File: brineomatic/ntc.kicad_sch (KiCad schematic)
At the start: 4 parts, among them J3 THERMISTOR

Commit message: starting to shape up, footprints etc
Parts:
- J4: renamed from J3; footprint (none) -> TerminalBlock_Phoenix:TerminalBlock_Phoenix_PT-1,5-2-3.5-H_1x02_P3.50mm_Horizontal
- renumbered R8 to R10, R7 to R9
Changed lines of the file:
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@@
 		(dnp no)
 		(fields_autoplaced yes)
-		(property "Reference" "J3"
+		(property "Reference" "J4"
 			(at 102.87 77.47 0)
 			(effects
@@
 			)
 		)
-		(property "Footprint" ""
+		(property "Footprint" "TerminalBlock_Phoenix:TerminalBlock_Phoenix_PT-1,5-2-3.5-H_1x02_P3.50mm_Horizontal"
 			(at 102.87 83.82 0)
 			(effects
@@
 			(project ""
 				(path "/96477ae2-ef08-48f3-8dd4-fe4478541f68/a25af3cd-6e30-4758-861f-193b34fc4628"
-					(reference "J3")
+					(reference "J4")
 					(unit 1)
 				)
@@
 		(dnp no)
 		(fields_autoplaced yes)
-		(property "Reference" "#PWR09"
+		(property "Reference" "#PWR014"
 			(at 118.11 113.03 0)
 			(effects
@@
 			(project "brineomatic"
 				(path "/96477ae2-ef08-48f3-8dd4-fe4478541f68/a25af3cd-6e30-4758-861f-193b34fc4628"
-					(reference "#PWR09")
+					(reference "#PWR014")
 					(unit 1)
 				)
@@
 		(dnp no)
 		(fields_autoplaced yes)
-		(property "Reference" "R8"
+		(property "Reference" "R10"
 			(at 118.11 80.01 90)
 			(effects
@@
 			(project "brineomatic"
 				(path "/96477ae2-ef08-48f3-8dd4-fe4478541f68/a25af3cd-6e30-4758-861f-193b34fc4628"
-					(reference "R8")
+					(reference "R10")
 					(unit 1)
 				)
@@
 		(dnp no)
 		(fields_autoplaced yes)
-		(property "Reference" "R7"
+		(property "Reference" "R9"
 			(at 114.3 93.98 0)
 			(effects
@@
 			(project "brineomatic"
 				(path "/96477ae2-ef08-48f3-8dd4-fe4478541f68/a25af3cd-6e30-4758-861f-193b34fc4628"
-					(reference "R7")
+					(reference "R9")
 					(unit 1)
 				)
@@
 		(dnp no)
 		(fields_autoplaced yes)
-		(property "Reference" "#PWR08"
+		(property "Reference" "#PWR013"
 			(at 111.76 78.74 0)
 			(effects
@@
 			(project ""
 				(path "/96477ae2-ef08-48f3-8dd4-fe4478541f68/a25af3cd-6e30-4758-861f-193b34fc4628"
-					(reference "#PWR08")
-					(unit 1)
-				)
+					(reference "#PWR013")
+					(unit 1)
+				)

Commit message: starting to look good.
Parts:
- J4: footprint TerminalBlock_Phoenix:TerminalBlock_Phoenix_PT-1,5-2-3.5-H_1x02_P3.50mm_Horizontal -> Connector_JST:JST_PH_S2B-PH-K_1x02_P2.00mm_Horizontal
- R9: footprint Resistor_SMD:R_1206_3216Metric_Pad1.30x1.75mm_HandSolder -> Resistor_SMD:R_0805_2012Metric_Pad1.20x1.40mm_HandSolder
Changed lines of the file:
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@@
 			)
 		)
-		(property "Footprint" "TerminalBlock_Phoenix:TerminalBlock_Phoenix_PT-1,5-2-3.5-H_1x02_P3.50mm_Horizontal"
+		(property "Footprint" "Connector_JST:JST_PH_S2B-PH-K_1x02_P2.00mm_Horizontal"
 			(at 102.87 83.82 0)
 			(effects
@@
 			)
 		)
-		(property "Footprint" "Resistor_SMD:R_1206_3216Metric_Pad1.30x1.75mm_HandSolder"
+		(property "Footprint" "Resistor_SMD:R_0805_2012Metric_Pad1.20x1.40mm_HandSolder"
 			(at 111.76 95.25 0)
 			(effects

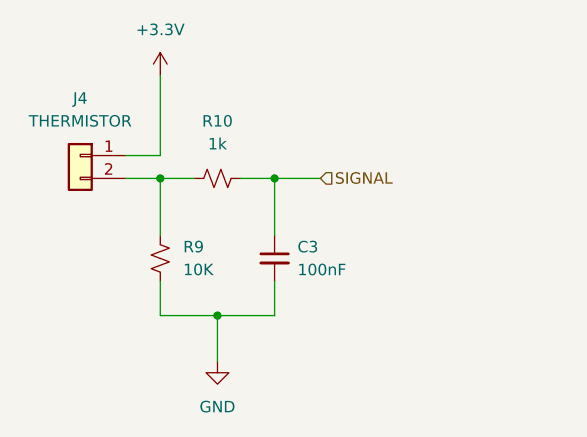
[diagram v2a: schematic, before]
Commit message: updated bom and prepping for Rev A
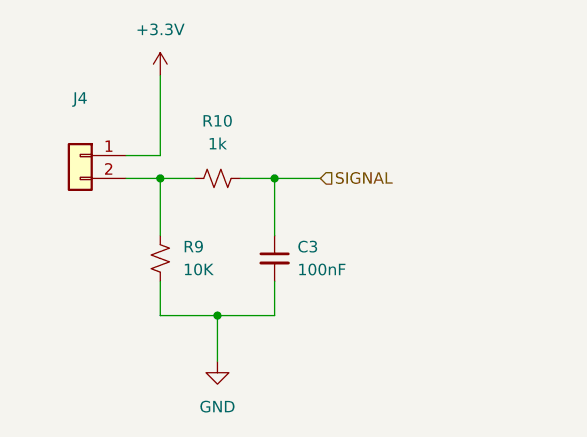
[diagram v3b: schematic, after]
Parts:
- J4: value THERMISTOR -> ~; LCSC (none) -> C173752
- R9: LCSC (none) -> C84376
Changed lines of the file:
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@@
 			)
 		)
-		(property "Value" "THERMISTOR"
+		(property "Value" "~"
 			(at 102.87 80.01 0)
 			(effects
@@
 		)
 		(property "Description" "Generic connector, single row, 01x02, script generated (kicad-library-utils/schlib/autogen/connector/)"
+			(at 102.87 83.82 0)
+			(effects
+				(font
+					(size 1.27 1.27)
+				)
+				(hide yes)
+			)
+		)
+		(property "LCSC" "C173752"
 			(at 102.87 83.82 0)
 			(effects
@@
 			)
 		)
-		(property "LCSC" ""
+		(property "LCSC" "C84376"
 			(at 111.76 95.25 0)
 			(effects

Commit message: fixed bat54s placement.
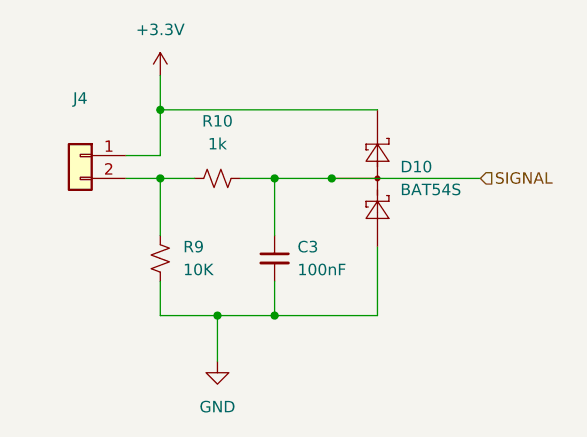
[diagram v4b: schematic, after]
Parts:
- added D10: BAT54S, Package_TO_SOT_SMD:SOT-23, symbol Diode:BAT54S
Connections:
- net +3.3V: now also D10.2 (K)
- net GND: now also D10.1 (A)
- net SIGNAL: now also D10.3 (COM)
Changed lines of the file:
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@@
+	)
+	(junction
+		(at 111.76 78.74)
+		(diameter 0)
+		(color 0 0 0 0)
+	)
+	(junction
+		(at 124.46 101.6)
+		(diameter 0)
+		(color 0 0 0 0)
 	)
 	(junction
@@
 		(color 0 0 0 0)
 	)
+	(junction
+		(at 130.81 86.36)
+		(diameter 0)
+		(color 0 0 0 0)
+	)
+	(wire
+		(pts
+			(xy 111.76 78.74) (xy 111.76 83.82)
+		)
+		(stroke
+			(width 0)
+			(type default)
+		)
+	)
 	(wire
 		(pts
@@
 	(wire
 		(pts
+			(xy 111.76 78.74) (xy 135.89 78.74)
+		)
+		(stroke
+			(width 0)
+			(type default)
+		)
+	)
+	(wire
+		(pts
 			(xy 118.11 101.6) (xy 124.46 101.6)
 		)
@@
 	(wire
 		(pts
-			(xy 111.76 74.93) (xy 111.76 83.82)
+			(xy 111.76 74.93) (xy 111.76 78.74)
 		)
 		(stroke
@@
 	(wire
 		(pts
-			(xy 124.46 86.36) (xy 129.54 86.36)
+			(xy 124.46 86.36) (xy 130.81 86.36)
 		)
 		(stroke
@@
 	(wire
 		(pts
+			(xy 130.81 86.36) (xy 147.32 86.36)
+		)
+		(stroke
+			(width 0)
+			(type default)
+		)
+	)
+	(wire
+		(pts
 			(xy 118.11 106.68) (xy 118.11 101.6)
+		)
+		(stroke
+			(width 0)
+			(type default)
+		)
+	)
+	(wire
+		(pts
+			(xy 135.89 93.98) (xy 135.89 101.6)
+		)
+		(stroke
+			(width 0)
+			(type default)
+		)
+	)
+	(wire
+		(pts
+			(xy 135.89 101.6) (xy 124.46 101.6)
 		)
 		(stroke
@@
 	(hierarchical_label "SIGNAL"
 		(shape input)
-		(at 129.54 86.36 0)
+		(at 147.32 86.36 0)
 		(fields_autoplaced yes)
 		(effects
@@
 					(unit 1)
 				)
+			)
+		)
+	)
+	(symbol
+		(lib_id "Diode:BAT54S")
+		(at 135.89 86.36 270)
+		(mirror x)
+		(unit 1)
+		(exclude_from_sim no)
+		(in_bom yes)
+		(on_board yes)
+		(dnp no)
+		(fields_autoplaced yes)
+		(property "Reference" "D10"
+			(at 138.43 85.09 90)
+			(effects
+				(font
+					(size 1.27 1.27)
+				)
+				(justify left)
+			)
+		)
+		(property "Value" "BAT54S"
+			(at 138.43 87.63 90)
+			(effects
+				(font
+					(size 1.27 1.27)
+				)
+				(justify left)
+			)
+		)
+		(property "Footprint" "Package_TO_SOT_SMD:SOT-23"
+			(at 139.065 84.455 0)
+			(effects
+				(font
+					(size 1.27 1.27)
+				)
+				(justify left)
+				(hide yes)
+			)
+		)
+		(property "Datasheet" "https://www.diodes.com/assets/Datasheets/ds11005.pdf"
+			(at 135.89 89.408 0)
+			(effects
+				(font
+					(size 1.27 1.27)
+				)
+				(hide yes)
+			)
+		)
+		(property "Description" ""
+			(at 135.89 86.36 0)
+			(effects
+				(font
+					(size 1.27 1.27)
+				)
+				(hide yes)
+			)
+		)
+		(property "LCSC" "C727126"
+			(at 135.89 86.36 90)
+			(effects
+				(font
+					(size 1.27 1.27)
+				)
+				(hide yes)
+			)
+		)
+		(pin "1"
+		)
+		(pin "2"
+		)
+		(pin "3"
+		)
+		(instances
+			(project "brineomatic"
+				(path "/96477ae2-ef08-48f3-8dd4-fe4478541f68/a25af3cd-6e30-4758-861f-193b34fc4628"
+					(reference "D10")
+					(unit 1)
+				)
